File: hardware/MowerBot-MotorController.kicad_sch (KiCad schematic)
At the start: 15 parts, among them J1 BTS7960_Left, J2 BTS7960_Right, J3 Encoder_Left, J4 Encoder_Right, J6 I2C_Expansion, J7 12V_Input, U1A ESP32_Left, U1B ESP32_Right, U2 LM2596_Module

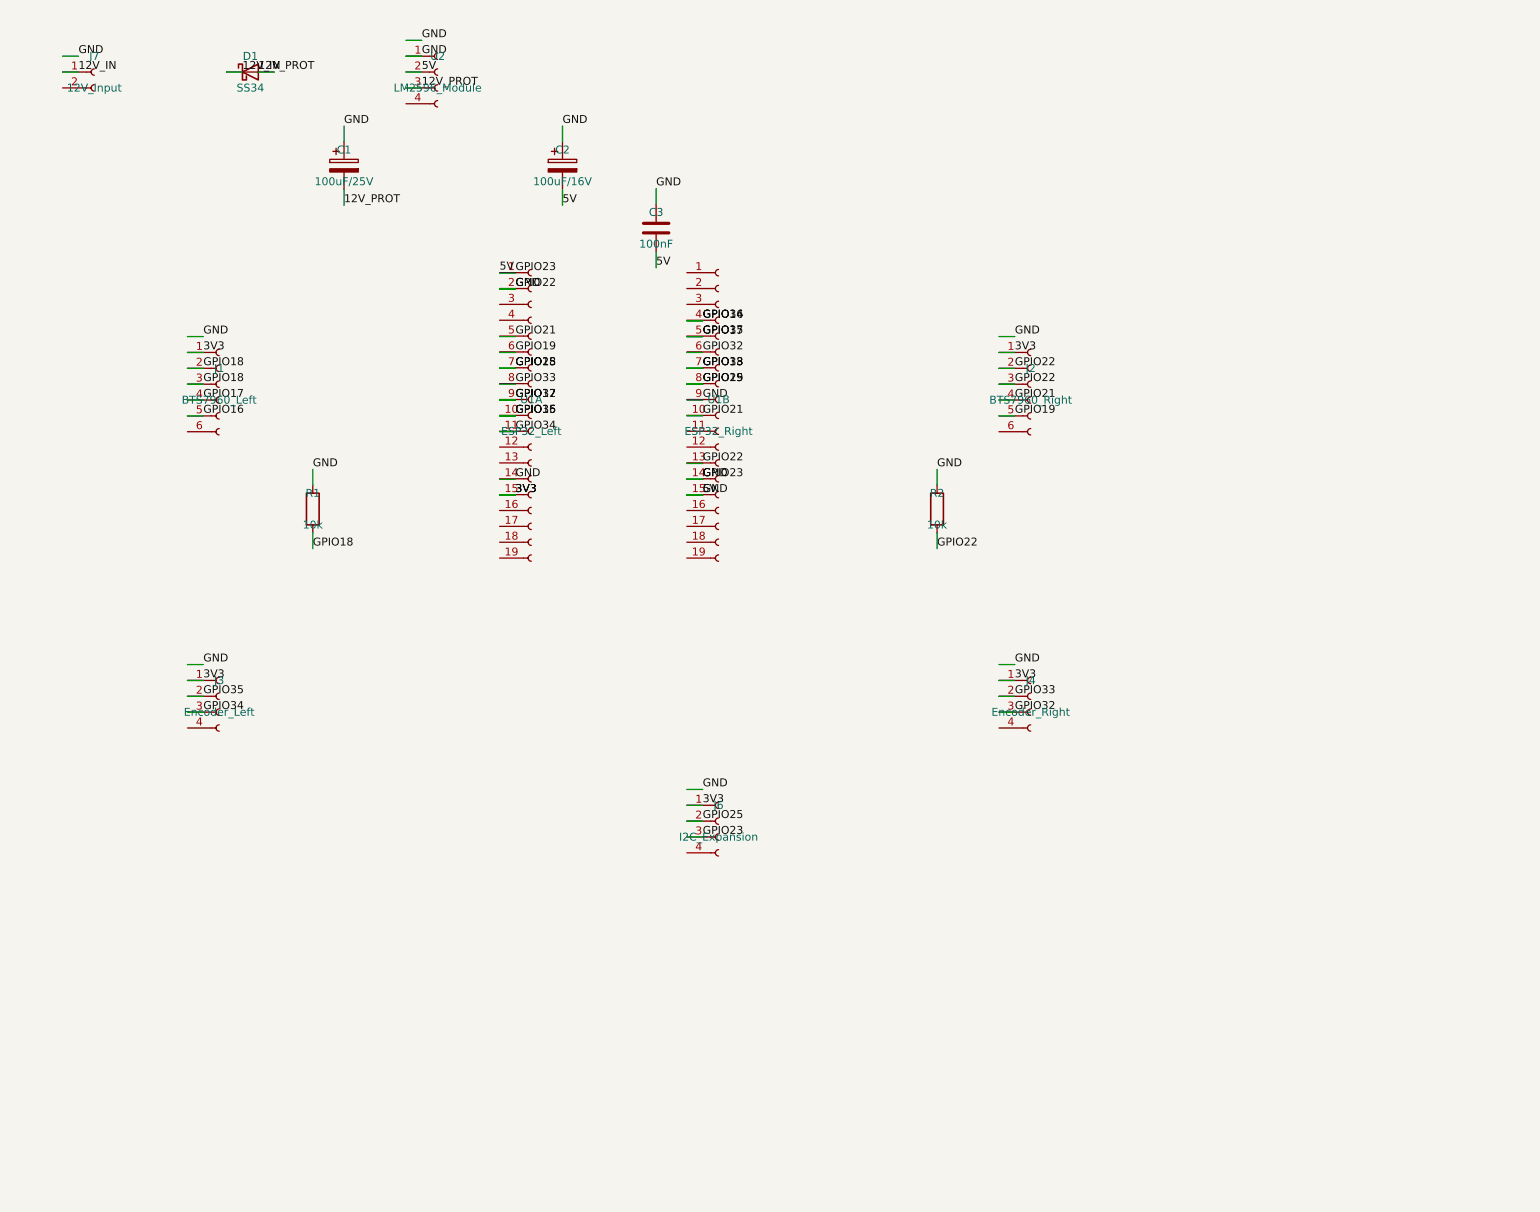
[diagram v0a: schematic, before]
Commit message: feat: redesign PCB as Raspberry Pi HAT v2.0 (65x100mm)
Complete KiCad project redesign for Raspberry Pi HAT form factor.

Board specifications:
- Size: 65x100mm (Pi HAT width, extended length)
- 6x M2.5 mounting holes (4 Pi HAT standard + 2 chassis support)
- GND copper pour on B.Cu
- Stacking header for Pi GPIO pass-through

Components (15 total):
- J_PI: 2x20 Pin Socket (40-pin Stacking Header for Pi GPIO)
- U1A/U1B: 2x 1x15 Pin Socket (ESP32-C3-DevKitM-1)
- J_SIG_L/R: 1x6 Pin Header (BTS7960 signal connectors)
- J_PWR_L/R: 2-pin Screw Terminal (BTS7960 12V power, 5.08mm)
- J_ENC_L/R: 1x4 Pin Header (encoder connectors)
- J7: 2-pin Screw Terminal (12V input from XT60 cable)
- U2: 1x4 Pin Header (MINI560 5V/5A step-down module)
- C1: 100uF/25V electrolytic (12V buffer)
- C2: 100uF/16V electrolytic (5V buffer)
- C3: 100nF ceramic (ESP32 VIN decoupling)
- R1/R2: 10k resistors (pull-down for motor enable safety)

Net assignments:
- 12V, 5V, 3V3, GND power rails
- PI_TXD, PI_RXD (UART between Pi and ESP32-C3)
- MOT_L_RPWM, MOT_L_LPWM, MOT_L_EN (left motor)
- MOT_R_RPWM, MOT_R_LPWM, MOT_R_EN (right motor)
- ENC_L_A, ENC_L_B, ENC_R_A, ENC_R_B (encoders)

Note: Schematic net labels are placed but may need manual
refinement in KiCad. Traces need routing (Freerouting or manual).
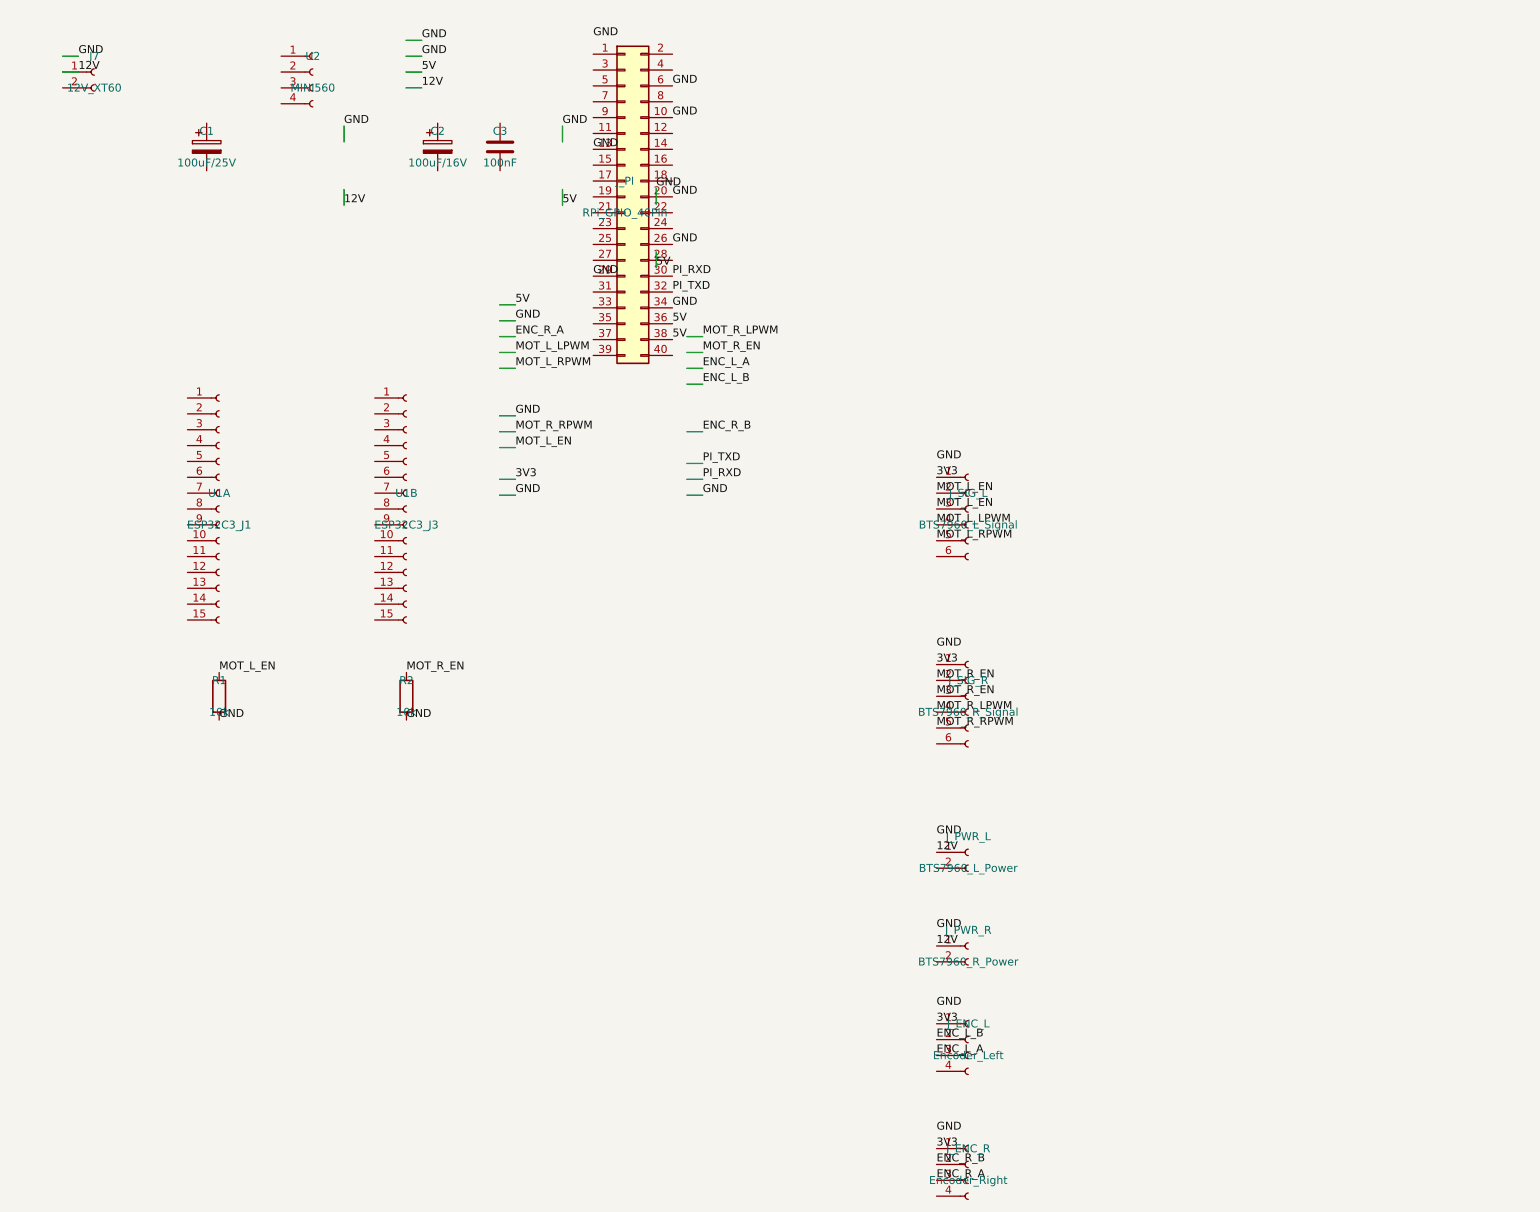
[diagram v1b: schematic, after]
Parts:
- removed D1: SS34, symbol Diode:SS34
- removed J1: BTS7960_Left, symbol Connector:Conn_01x06_Socket
- removed J2: BTS7960_Right, symbol Connector:Conn_01x06_Socket
- removed J3: Encoder_Left, symbol Connector:Conn_01x04_Socket
- removed J4: Encoder_Right, symbol Connector:Conn_01x04_Socket
- removed J6: I2C_Expansion, symbol Connector:Conn_01x04_Socket
- removed U1A: ESP32_Left, symbol Connector:Conn_01x19_Socket
- removed U1B: ESP32_Right, symbol Connector:Conn_01x19_Socket
- added J_ENC_L: Encoder_Left, symbol Connector:Conn_01x04_Socket
- added J_ENC_R: Encoder_Right, symbol Connector:Conn_01x04_Socket
- added J_PI: RPi_GPIO_40Pin, symbol Connector_Generic:Conn_02x20_Odd_Even
- added J_PWR_L: BTS7960_L_Power, symbol Connector:Conn_01x02_Socket
- added J_PWR_R: BTS7960_R_Power, symbol Connector:Conn_01x02_Socket
- added J_SIG_L: BTS7960_L_Signal, symbol Connector:Conn_01x06_Socket
- added J_SIG_R: BTS7960_R_Signal, symbol Connector:Conn_01x06_Socket
- added U1A: ESP32C3_J1, symbol Connector:Conn_01x15_Socket
- added U1B: ESP32C3_J3, symbol Connector:Conn_01x15_Socket
- J7: value 12V_Input -> 12V_XT60
- U2: value LM2596_Module -> MINI560
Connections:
- net 3V3: now also J_ENC_L.1 (Pin_1), J_ENC_R.1 (Pin_1), J_SIG_L.1 (Pin_1), J_SIG_R.1 (Pin_1)
- net 5V: now also J_PI.36 (Pin_36), J_PI.38 (Pin_38); no longer C1.1, C2.1, C2.2, C3.1, C3.2, R1.1, R2.1, R2.2, U2.1 (Pin_1), U2.2 (Pin_2)
- net 12V_IN renamed 12V
- net 12V: now also J_PWR_L.1 (Pin_1), J_PWR_R.1 (Pin_1)
- net 12V_PROT: no longer names the net of C1.2
- net 12V_PROT: no longer U2.3 (Pin_3)
- net GPIO18 renamed GND
- net GND: now also R2.2, J_PI.10 (Pin_10), J_PI.13 (Pin_13), J_PI.20 (Pin_20), J_PI.26 (Pin_26), J_PI.29 (Pin_29), J_PI.34 (Pin_34), J_PI.6 (Pin_6)
- new net ENC_L_A: J_ENC_L.3 (Pin_3)
- new net ENC_L_B: J_ENC_L.2 (Pin_2)
- new net ENC_R_A: J_ENC_R.3 (Pin_3)
- new net ENC_R_B: J_ENC_R.2 (Pin_2)
- new net MOT_L_EN: J_SIG_L.2 (Pin_2), J_SIG_L.3 (Pin_3), R1.1
- new net MOT_L_LPWM: J_SIG_L.4 (Pin_4)
- new net MOT_L_RPWM: J_SIG_L.5 (Pin_5)
- new net MOT_R_EN: J_SIG_R.2 (Pin_2), J_SIG_R.3 (Pin_3), R2.1
- new net MOT_R_LPWM: J_SIG_R.4 (Pin_4)
- new net MOT_R_RPWM: J_SIG_R.5 (Pin_5)
- new net PI_RXD: J_PI.30 (Pin_30)
- new net PI_TXD: J_PI.32 (Pin_32)

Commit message: feat(hardware): MowerBot HAT v2.0 motor controller PCB sources
Commit the KiCad project + symbol/footprint libraries + 3D models +
fabrication output for the v2.0 motor controller HAT. Source files
have been live in the working tree since early April but never
committed.

Includes:
- kicad_pcb / kicad_sch / kicad_pro / kicad_prl
- MowerBot.kicad_sym + MowerBot.pretty/ (custom footprints)
- 3D models (ADS1115, BTS7960, GY521 MPU6050, MINI560)
- Schematic PDF + DRC violations report
- production/ (Gerbers, BOM, positions, IPC netlist)
- fabrication-toolkit-options.json
- docs/pcb-motor-controller.md updates
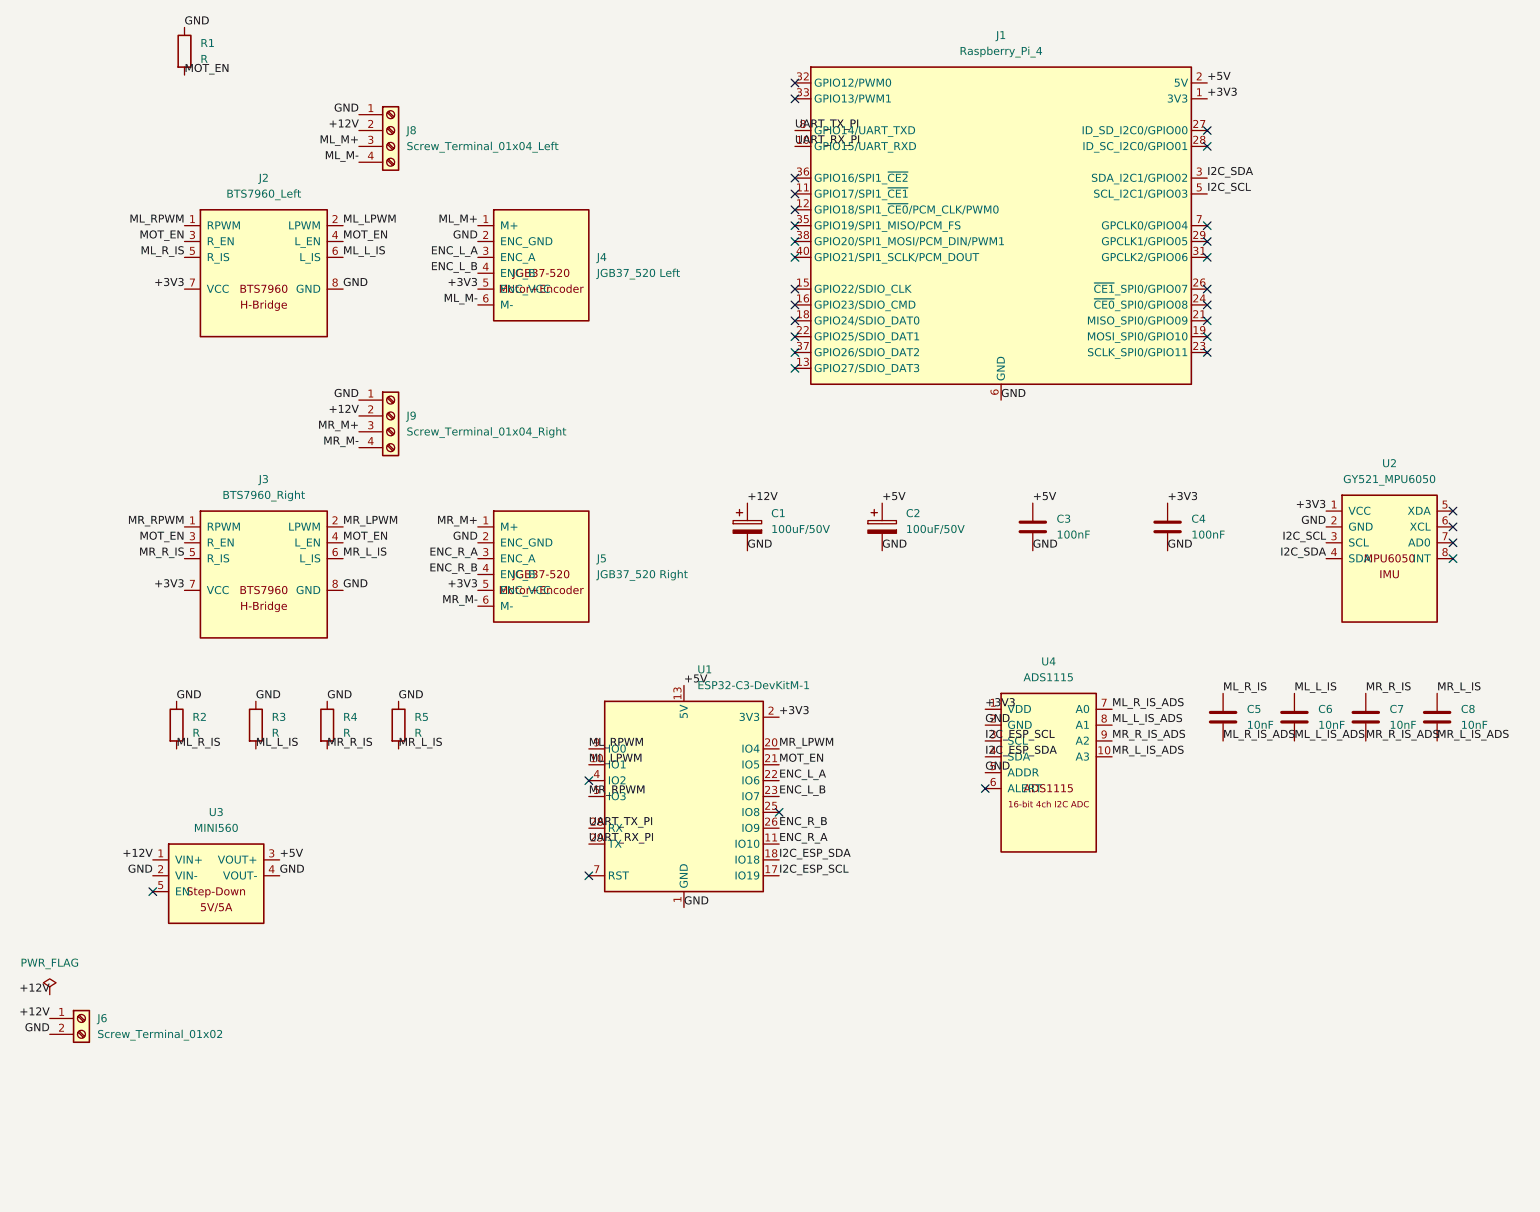
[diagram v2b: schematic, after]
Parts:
- removed J7: 12V_XT60, symbol Connector:Conn_01x02_Socket
- removed J_ENC_L: Encoder_Left, symbol Connector:Conn_01x04_Socket
- removed J_ENC_R: Encoder_Right, symbol Connector:Conn_01x04_Socket
- removed J_PI: RPi_GPIO_40Pin, symbol Connector_Generic:Conn_02x20_Odd_Even
- removed J_PWR_L: BTS7960_L_Power, symbol Connector:Conn_01x02_Socket
- removed J_PWR_R: BTS7960_R_Power, symbol Connector:Conn_01x02_Socket
- removed J_SIG_L: BTS7960_L_Signal, symbol Connector:Conn_01x06_Socket
- removed J_SIG_R: BTS7960_R_Signal, symbol Connector:Conn_01x06_Socket
- removed U1A: ESP32C3_J1, symbol Connector:Conn_01x15_Socket
- removed U1B: ESP32C3_J3, symbol Connector:Conn_01x15_Socket
- removed U2: MINI560, symbol Connector:Conn_01x04_Socket
- added C4: 100nF, Capacitor_SMD:C_0805_2012Metric, symbol Device:C
- added C5, C6, C7, C8: 10nF, Capacitor_SMD:C_0805_2012Metric, symbol Device:C
- added J1: Raspberry_Pi_4, Connector_PinSocket_2.54mm:PinSocket_2x20_P2.54mm_Vertical, symbol Connector:Raspberry_Pi_4
- added J2: BTS7960_Left, MowerBot:BTS7960, symbol MowerBot:BTS7960
- added J3: BTS7960_Right, MowerBot:BTS7960, symbol MowerBot:BTS7960
- added J4: JGB37_520 Left, MowerBot:JGB37_520, symbol MowerBot:JGB37_520
- added J5: JGB37_520 Right, MowerBot:JGB37_520, symbol MowerBot:JGB37_520
- added J6: Screw_Terminal_01x02, TerminalBlock_Phoenix:TerminalBlock_Phoenix_MKDS-1,5-2-5.08_1x02_P5.08mm_Horizontal, symbol Connector:Screw_Terminal_01x02
- added J8: Screw_Terminal_01x04_Left, TerminalBlock_Phoenix:TerminalBlock_Phoenix_MKDS-1,5-4-5.08_1x04_P5.08mm_Horizontal, symbol Connector:Screw_Terminal_01x04
- added J9: Screw_Terminal_01x04_Right, TerminalBlock_Phoenix:TerminalBlock_Phoenix_MKDS-1,5-4-5.08_1x04_P5.08mm_Horizontal, symbol Connector:Screw_Terminal_01x04
- added R3, R4, R5: R, Resistor_SMD:R_0805_2012Metric, symbol Device:R
- added U1: ESP32-C3-DevKitM-1, RF_Module:ESP32-C3-DevKitM-1, symbol RF_Module:ESP32-C3-DevKitM-1
- added U2: GY521_MPU6050, MowerBot:GY521_MPU6050, symbol MowerBot:GY521_MPU6050
- added U3: MINI560, MowerBot:MINI560, symbol MowerBot:MINI560
- added U4: ADS1115, MowerBot:ADS1115, symbol MowerBot:ADS1115
- C1: value 100uF/25V -> 100uF/50V; footprint (none) -> Capacitor_THT:CP_Radial_D8.0mm_P3.50mm
- C2: value 100uF/16V -> 100uF/50V; footprint (none) -> Capacitor_THT:CP_Radial_D8.0mm_P3.50mm
- C3: footprint (none) -> Capacitor_SMD:C_0805_2012Metric
- R1, R2: value 10k -> R; footprint (none) -> Resistor_SMD:R_0805_2012Metric
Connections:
- net MOT_L_EN is gone; now on net GND: R1.1
- net MOT_R_EN is gone; now on net GND: R2.1
- net ENC_L_A: now also J4.3 (ENC_A), U1.22 (IO6)
- net ENC_L_B: now also J4.4 (ENC_B), U1.23 (IO7)
- net ENC_R_A: now also J5.3 (ENC_A), U1.11 (IO10)
- net ENC_R_B: now also J5.4 (ENC_B), U1.26 (IO9)
- net GND: now also C1.2, C2.2, C3.2, C4.2, J1.14 (GND), J1.20 (GND), J1.25 (GND), J1.30 (GND), J1.34 (GND), J1.39 (GND), J1.6 (GND), J1.9 (GND), J2.8 (GND), J3.8 (GND), J4.2 (ENC_GND), J5.2 (ENC_GND), J6.2 (Pin_2), J8.1 (Pin_1), J9.1 (Pin_1), R3.1, R4.1, R5.1, U1.1 (GND), U1.12 (GND), U1.15 (GND), U1.16 (GND), U1.19 (GND), U1.24 (GND), U1.27 (GND), U1.30 (GND), U1.6 (GND), U1.8 (GND), U2.2 (GND), U3.2 (VIN-), U3.4 (VOUT-), U4.2 (GND), U4.5 (ADDR); no longer R1.2, R2.2
- net +5V: now reaches C3.1
- net +5V: now also C2.1, J1.2 (5V), J1.4 (5V), U1.13 (5V), U1.14 (5V), U3.3 (VOUT+)
- net +12V: now reaches C1.1
- net +12V: now also J6.1 (Pin_1), J8.2 (Pin_2), J9.2 (Pin_2), U3.1 (VIN+)
- new net +3V3: C4.1, J1.1 (3V3), J1.17 (3V3), J2.7 (VCC), J3.7 (VCC), J4.5 (ENC_VCC), J5.5 (ENC_VCC), U1.2 (3V3), U1.3 (3V3), U2.1 (VCC), U4.1 (VDD)
- new net I2C_ESP_SCL: U1.17 (IO19), U4.3 (SCL)
- new net I2C_ESP_SDA: U1.18 (IO18), U4.4 (SDA)
- new net I2C_SCL: J1.5 (SCL_I2C1/GPIO03), U2.3 (SCL)
- new net I2C_SDA: J1.3 (SDA_I2C1/GPIO02), U2.4 (SDA)
- new net ML_LPWM: J2.2 (LPWM), U1.10 (IO1)
- new net ML_L_IS: C6.1, J2.6 (L_IS), R3.2
- new net ML_L_IS_ADS: C6.2, U4.8 (A1)
- new net ML_M+: J4.1 (M+), J8.3 (Pin_3)
- new net ML_M-: J4.6 (M-), J8.4 (Pin_4)
- new net ML_RPWM: J2.1 (RPWM), U1.9 (IO0)
- new net ML_R_IS: C5.1, J2.5 (R_IS), R2.2
- new net ML_R_IS_ADS: C5.2, U4.7 (A0)
- new net MOT_EN: J2.3 (R_EN), J2.4 (L_EN), J3.3 (R_EN), J3.4 (L_EN), R1.2, U1.21 (IO5)
- new net MR_LPWM: J3.2 (LPWM), U1.20 (IO4)
- new net MR_L_IS: C8.1, J3.6 (L_IS), R5.2
- new net MR_L_IS_ADS: C8.2, U4.10 (A3)
- new net MR_M+: J5.1 (M+), J9.3 (Pin_3)
- new net MR_M-: J5.6 (M-), J9.4 (Pin_4)
- new net MR_RPWM: J3.1 (RPWM), U1.5 (IO3)
- new net MR_R_IS: C7.1, J3.5 (R_IS), R4.2
- new net MR_R_IS_ADS: C7.2, U4.9 (A2)
- new net UART_RX_PI: J1.10 (GPIO15/UART_RXD), U1.29 (TX)
- new net UART_TX_PI: J1.8 (GPIO14/UART_TXD), U1.28 (RX)
- no-connect marks 0 -> 33
